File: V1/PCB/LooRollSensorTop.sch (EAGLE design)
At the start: 18 parts, among them Q1 200mA/50V, U1 HTU21DSMD

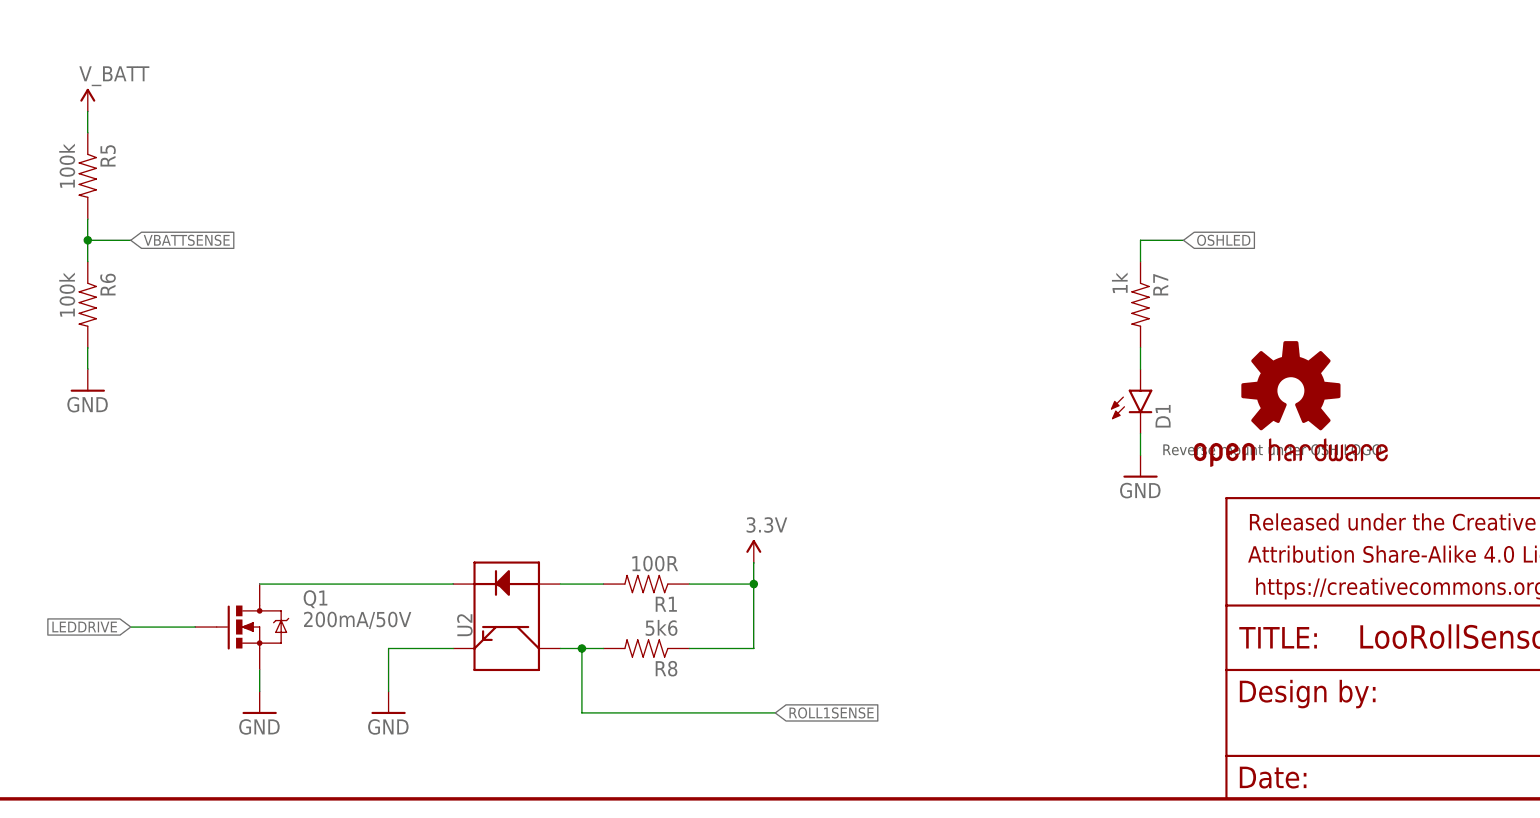
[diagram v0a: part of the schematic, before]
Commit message: Moved PCB files to a dedicated folder.
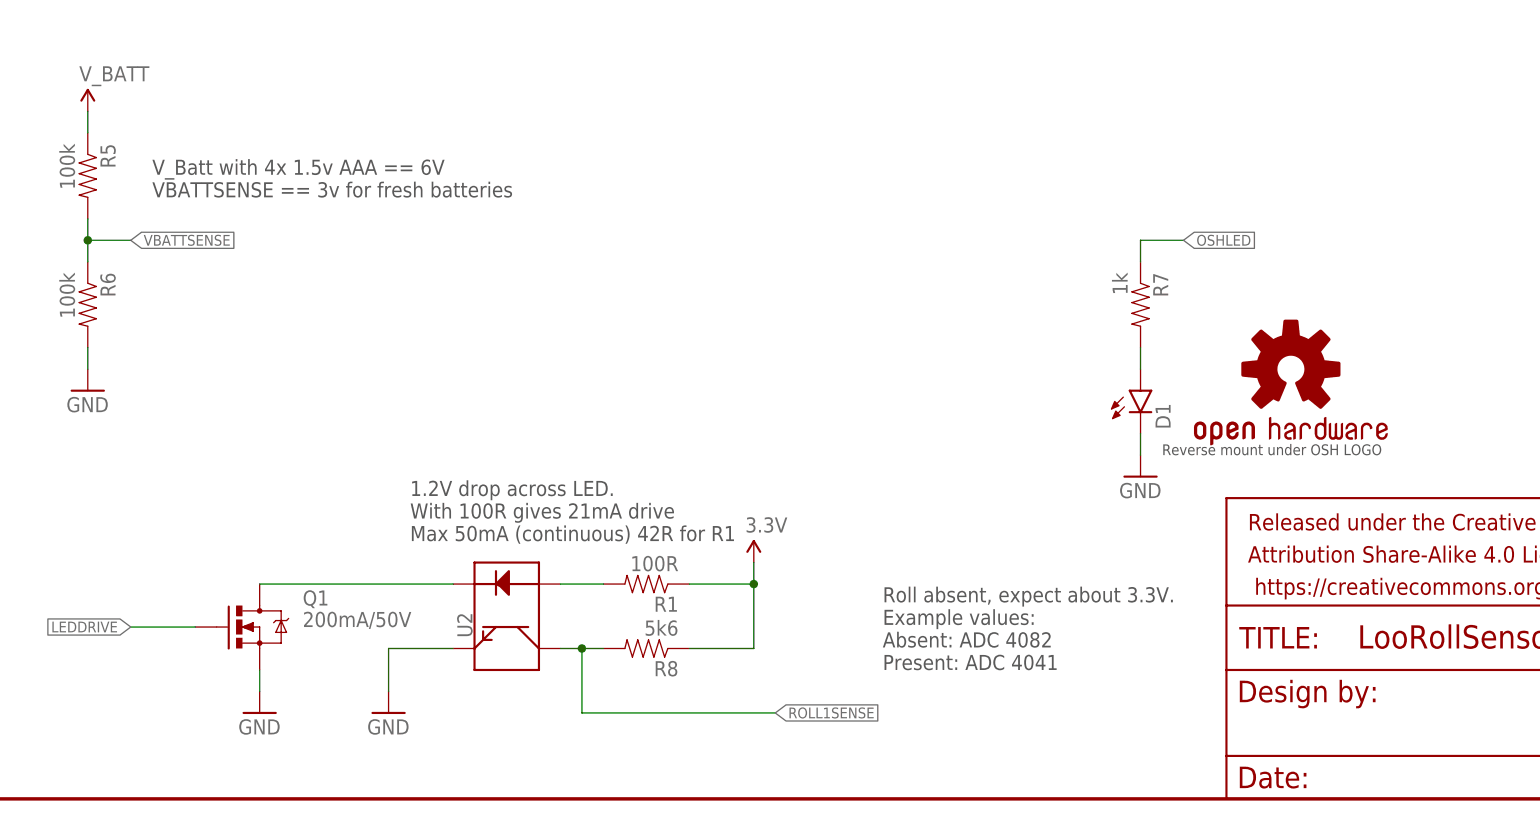
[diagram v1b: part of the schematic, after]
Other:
- note added: "1.2V drop across LED. With 100R gives 21mA drive Max 50mA (continuous) 42R for R1"
- note added: "Roll absent, expect about 3.3V. Example values: Absent: ADC 4082 Present: ADC 4041"
- note added: "V_Batt with 4x 1.5v AAA == 6V VBATTSENSE == 3v for fresh batteries"
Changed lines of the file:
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@@
 <text x="38.1" y="40.64" size="1.27" layer="97" rot="R90">TODO: Water sense should wake Photon when water is detected.</text>
 <text x="170.18" y="-38.1" size="1.27" layer="97">Reverse mount under OSH LOGO</text>
+<text x="81.28" y="-48.26" size="1.778" layer="97">1.2V drop across LED.
+With 100R gives 21mA drive
+Max 50mA (continuous) 42R for R1</text>
+<text x="137.16" y="-63.5" size="1.778" layer="97">Roll absent, expect about 3.3V.
+Example values:
+Absent: ADC 4082
+Present: ADC 4041</text>
+<text x="50.8" y="-7.62" size="1.778" layer="97">V_Batt with 4x 1.5v AAA == 6V
+VBATTSENSE == 3v for fresh batteries</text>
 </plain>
 <instances>
@@
 <instance part="GND11" gate="1" x="208.28" y="63.5"/>
 <instance part="SUPPLY9" gate="G$1" x="208.28" y="78.74"/>
-<instance part="LOGO1" gate="G$1" x="185.42" y="-30.48"/>
+<instance part="LOGO1" gate="G$1" x="185.42" y="-27.94"/>
 <instance part="U2" gate="&gt;NAME" x="93.98" y="-58.42" rot="MR90"/>
 <instance part="R8" gate="G$1" x="109.22" y="-60.96" rot="R180"/>

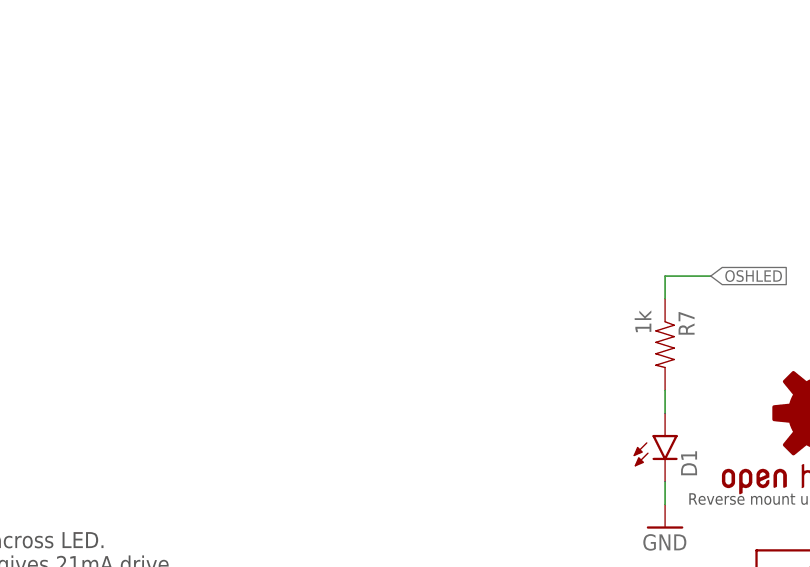
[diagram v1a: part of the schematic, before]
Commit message: Added bodge resistor required to pull LED drive low to prevent LEDs switching on when Photon is in power save mode.
"Printed" eagle files as pdfs.
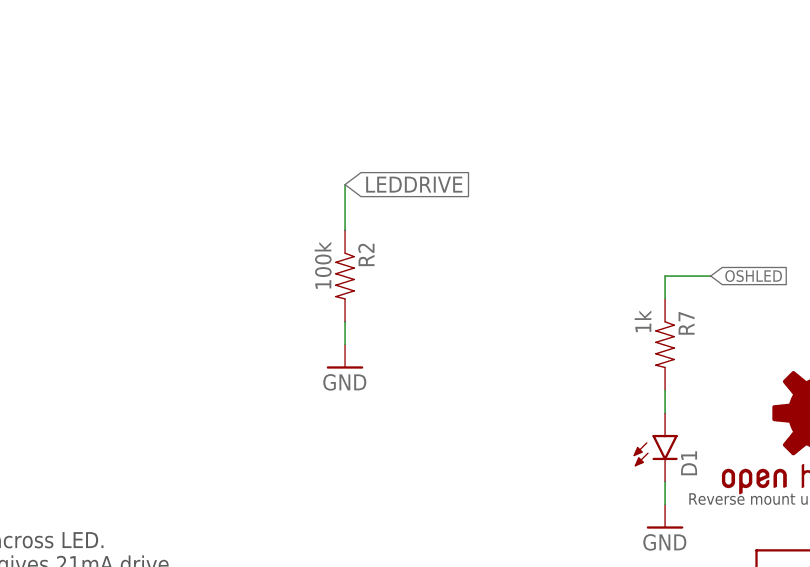
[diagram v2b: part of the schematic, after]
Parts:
- added R2: 100k, SparkFun-Resistors:RESISTOR1206
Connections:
- net GND: now also R2.2
- net LEDDRIVE: now also R2.1
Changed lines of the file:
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@@
 <part name="U2" library="SparkFun-Sensors" deviceset="QRE1113" device="SMD-W"/>
 <part name="R8" library="SparkFun-Resistors" deviceset="RESISTOR" device="1206" value="5k6"/>
+<part name="R2" library="SparkFun-Resistors" deviceset="RESISTOR" device="1206" value="100k"/>
+<part name="GND7" library="SparkFun-Aesthetics" deviceset="GND" device=""/>
 </parts>
 <sheets>
@@
 <instance part="U2" gate="&gt;NAME" x="93.98" y="-58.42" rot="MR90"/>
 <instance part="R8" gate="G$1" x="109.22" y="-60.96" rot="R180"/>
+<instance part="R2" gate="G$1" x="132.08" y="-12.7" rot="R270"/>
+<instance part="GND7" gate="1" x="132.08" y="-22.86"/>
 </instances>
 <busses>
@@
 <wire x1="208.28" y1="66.04" x2="208.28" y2="68.58" width="0.1524" layer="91"/>
 </segment>
+<segment>
+<pinref part="R2" gate="G$1" pin="2"/>
+<pinref part="GND7" gate="1" pin="GND"/>
+<wire x1="132.08" y1="-20.32" x2="132.08" y2="-17.78" width="0.1524" layer="91"/>
+</segment>
 </net>
 <net name="N$3" class="0">
@@
 <label x="264.16" y="25.4" size="1.27" layer="95" xref="yes"/>
 </segment>
-</net>
+<segment>
+<pinref part="R2" gate="G$1" pin="1"/>
+<wire x1="132.08" y1="-7.62" x2="132.08" y2="-2.54" width="0.1524" layer="91"/>
+<label x="132.08" y="-2.54" size="1.778" layer="95" xref="yes"/>
+</segment>
+</net>
